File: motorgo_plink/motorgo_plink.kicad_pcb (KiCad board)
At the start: 4 copper layers, 80.5 x 64.5 mm, 141 parts, among them J1 USB4520-03-0-A_REVA, J10 Conn_01x02_Pin, J13 I2C_STANDARDQWIIC, J14 BM05B-SRSS-TB_LF__SN_, J15 I2C_STANDARDQWIIC, J16 BM05B-SRSS-TB_LF__SN_, J17 I2C_STANDARDQWIIC, J18 BM05B-SRSS-TB_LF__SN_, J19 I2C_STANDARDQWIIC, J20 BM05B-SRSS-TB_LF__SN_, J22 Conn_01x02_Pin, J23 Conn_01x06_Pin, J4 Conn_02x20_Odd_Even, J5 Conn_02x20_Odd_Even, J6 Conn_01x02_Pin, J7 USB4520-03-0-A_REVA, J8 Conn_01x02_Pin, Q1 SI2323, U1 ESP32-S3-WROOM-1, U10 LIS3MDLTR, U11 LSM6DS3TR, U2 USBLC6-2P6, U3 DRV8874PWPR, U4 DRV8874PWPR, U5 DRV8874PWPR, U6 TPS54620RHLR, U7 HUSB238_002DD, U8 AMS1117-3.3, U9 DRV8874PWPR

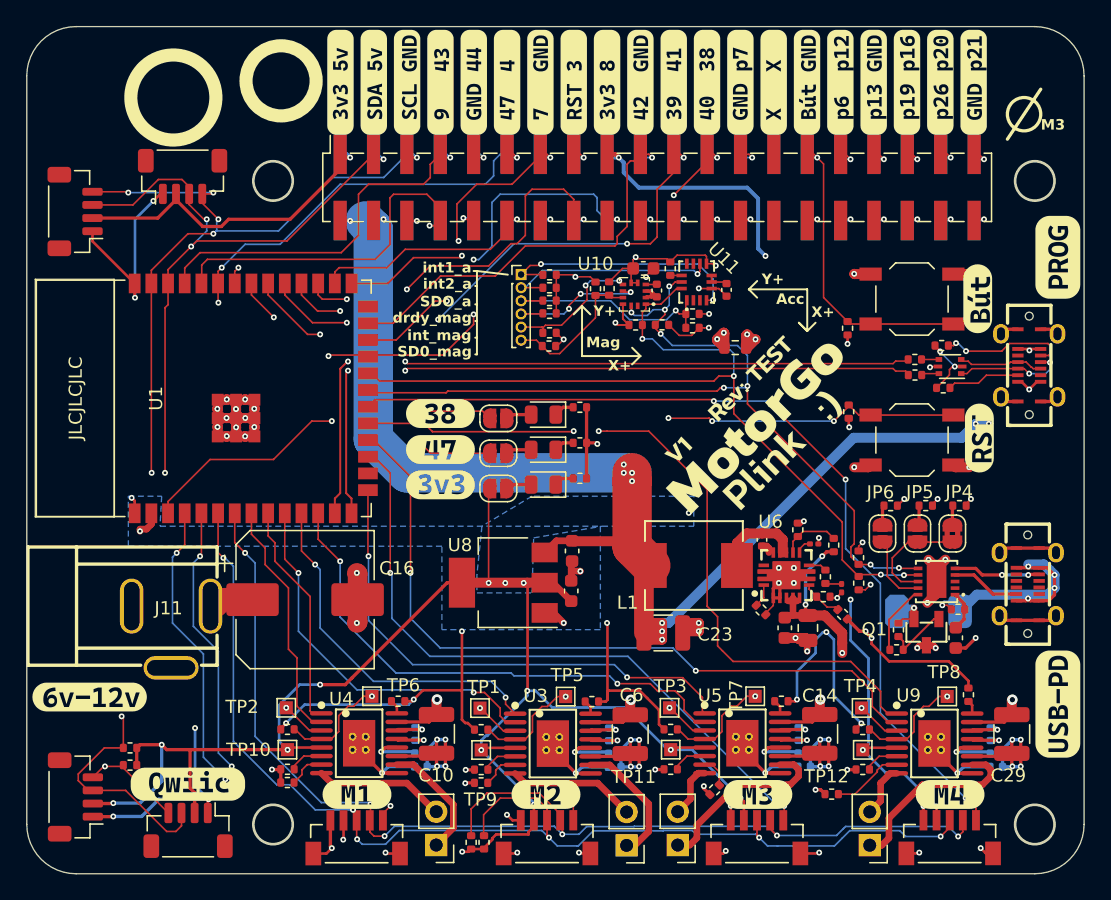
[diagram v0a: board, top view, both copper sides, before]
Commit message: wip culling schematics and removing tracks
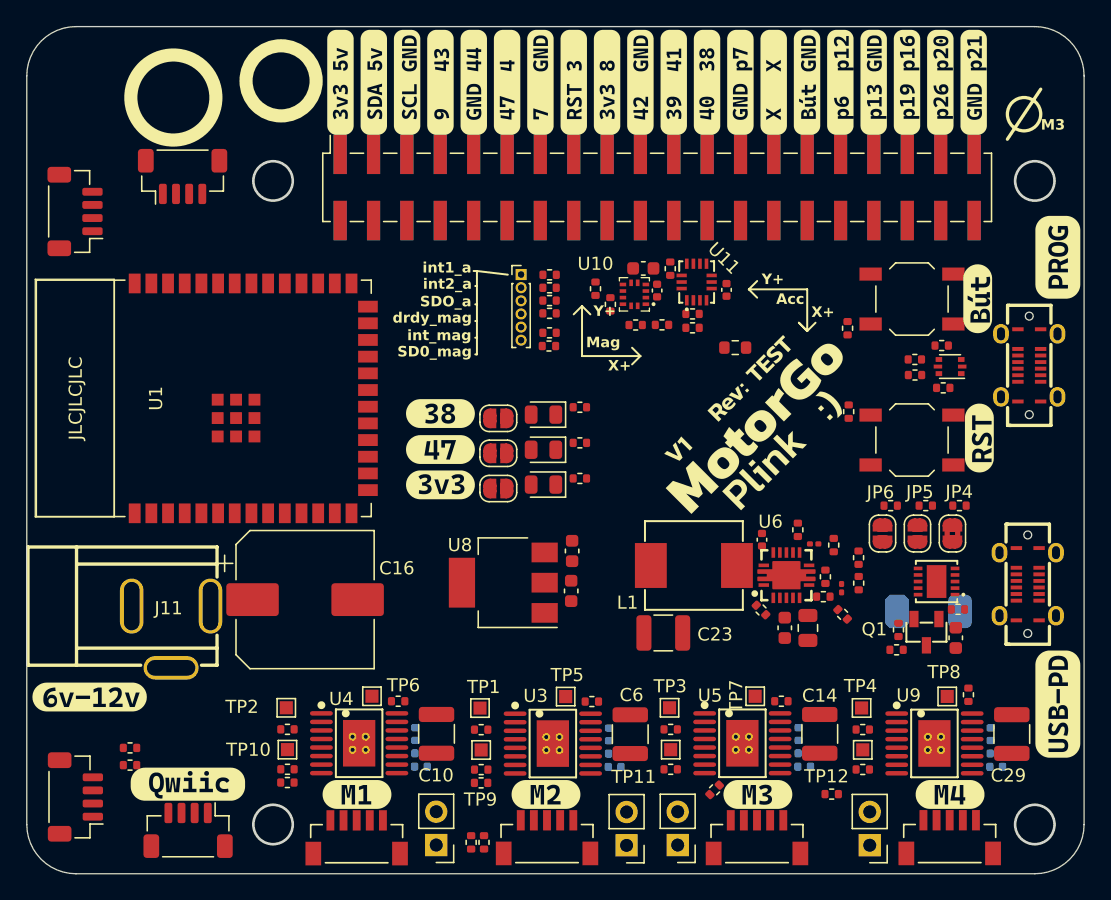
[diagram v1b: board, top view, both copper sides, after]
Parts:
- moved R47 1.21 mm to (138.7, 72.9), turned to -90 degrees
- turned C31 to -90 degrees
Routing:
- net +3.3V: track 248.3 -> 0.00 mm, vias 32 -> 0
- net GND: track 190.5 -> 0.00 mm, vias 83 -> 0
- net +5V: track 174.6 -> 0.00 mm, vias 23 -> 0
- net enc_scl: track 91.8 -> 0.00 mm, vias 6 -> 0
- net enc_sda: track 91.2 -> 0.00 mm, vias 6 -> 0
- net sda: track 88.5 -> 0.00 mm, vias 5 -> 0
- net scl: track 85.8 -> 0.00 mm, vias 7 -> 0
- net +BATT: track 80.2 -> 0.00 mm, vias 21 -> 0
- net hidden_sda: track 69.4 -> 0.00 mm, vias 8 -> 0
- net m4_enc_cs: track 69.2 -> 0.00 mm, vias 4 -> 0
- net hidden_scl: track 67.2 -> 0.00 mm, vias 4 -> 0
- net boot: track 64.4 -> 0.00 mm, vias 2 -> 0
- net reset: track 64.3 -> 0.00 mm, vias 4 -> 0
- net gpio47: track 56.8 -> 0.00 mm, vias 4 -> 0
- net m4_EN: track 56.6 -> 0.00 mm, vias 2 -> 0
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- removed copper zone on B.Cu, net +3.3V
- removed copper zone on In2.Cu, net +3.3V
- removed copper zone on In2.Cu, net +5V
- removed copper zone on In2.Cu, net +BATT
- removed copper zone on In2.Cu, net +VDC
- removed copper zone on In1.Cu, net GND
- removed copper zone on In1.Cu, net GNDD
